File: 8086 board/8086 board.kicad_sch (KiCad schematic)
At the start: 37 parts, among them J1 8086 bus, U1 P8086-2, U2 74HC32

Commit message: PCB: different layout
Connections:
- net BUSALE: now also J1.21 (Pin_21); no longer J1.27 (Pin_27)
- net HLDA: now also J1.25 (Pin_25); no longer J1.23 (Pin_23)
- net HOLD: now also J1.28 (Pin_28); no longer J1.22 (Pin_22)
- net M\~{IO}: now also J1.23 (Pin_23); no longer J1.25 (Pin_25)
- net READY: now also J1.24 (Pin_24); no longer J1.26 (Pin_26)
- net ~{BHE}: now also J1.22 (Pin_22); no longer J1.28 (Pin_28)
- net ~{RD}: now also J1.27 (Pin_27); no longer J1.21 (Pin_21)
- net ~{WR}: now also J1.26 (Pin_26); no longer J1.24 (Pin_24)

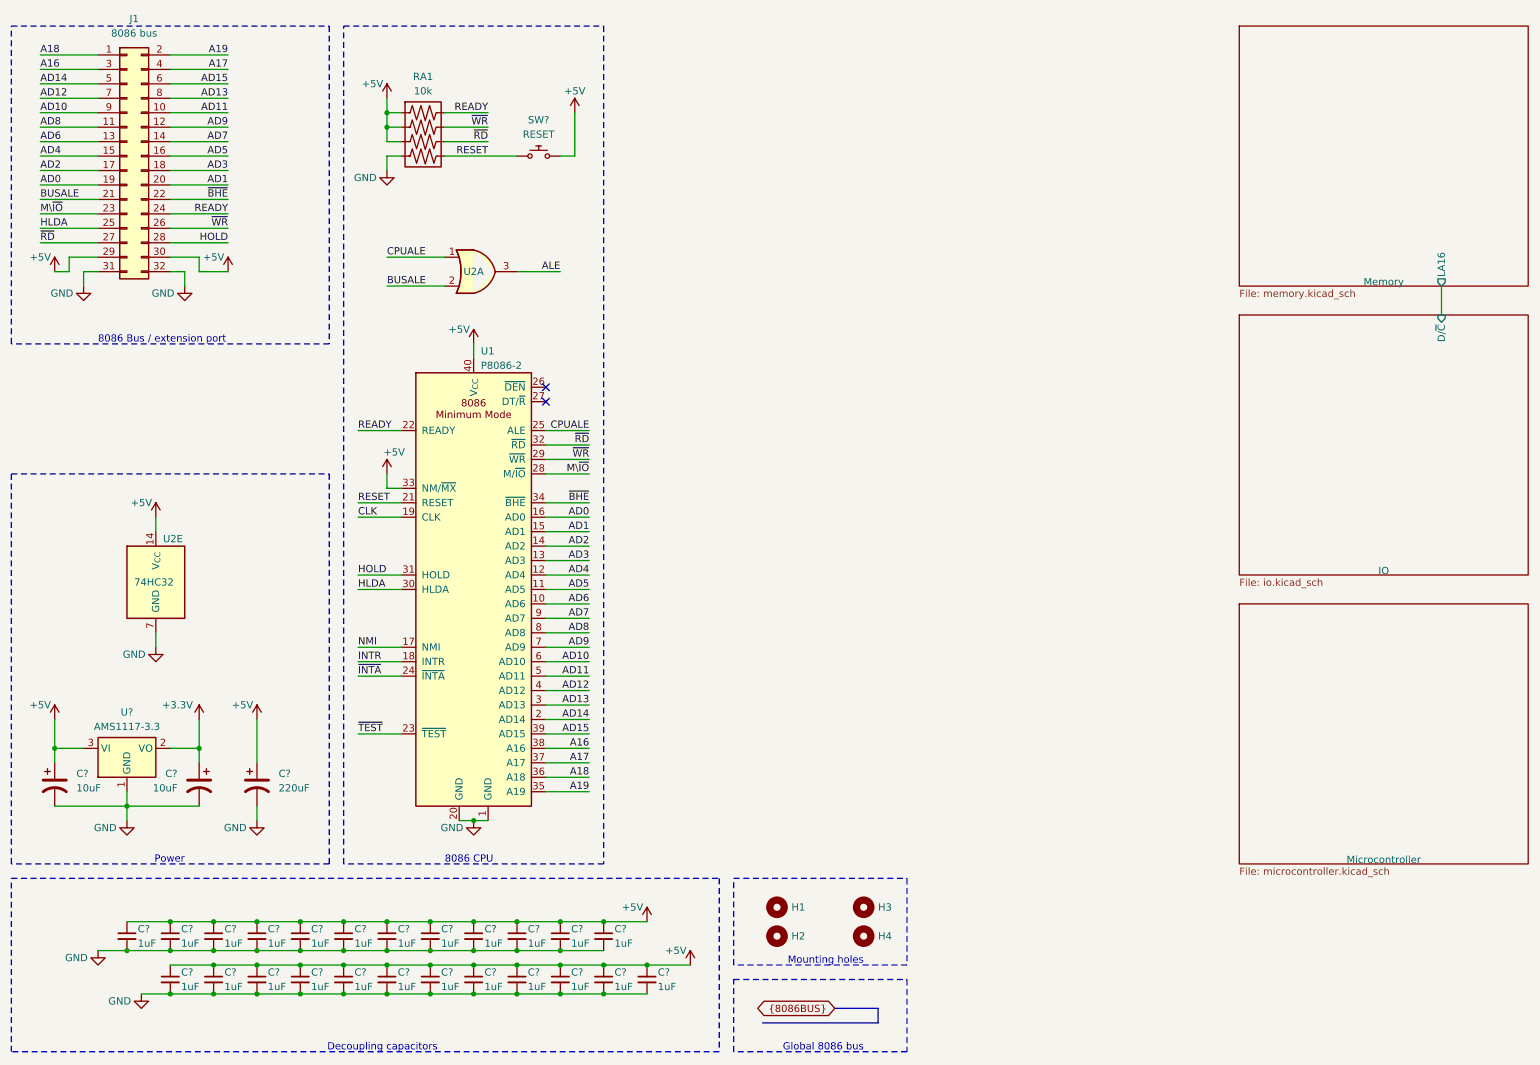
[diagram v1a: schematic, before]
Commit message: PCB: layout and routing of IO, shift registers, and MCU
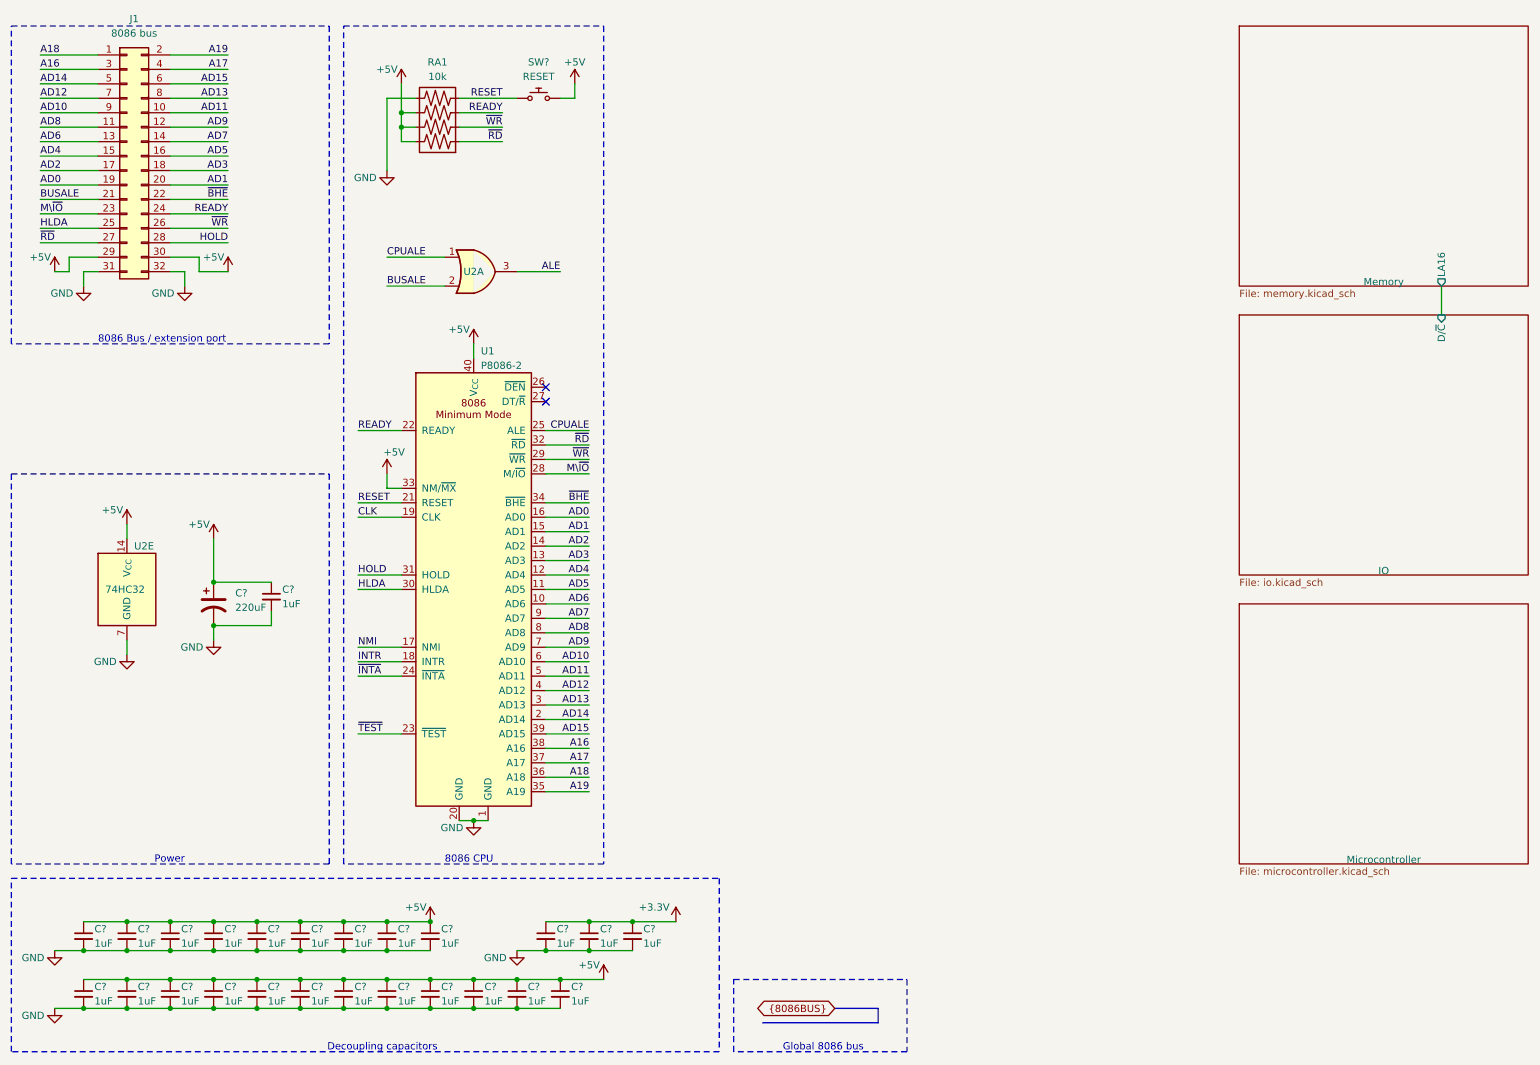
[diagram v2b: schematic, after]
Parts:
- removed C? (x2): 10uF, Capacitor_SMD:C_0603_1608Metric_Pad1.08x0.95mm_HandSolder, symbol Device:C_Polarized_US
- removed H1, H2, H3, H4: ~, MountingHole:MountingHole_3.2mm_M3, symbol Mechanical:MountingHole
- removed U?: AMS1117-3.3, Package_TO_SOT_SMD:SOT-223-3_TabPin2, symbol Regulator_Linear:AMS1117-3.3
- added C?: 1uF, Capacitor_SMD:C_0603_1608Metric_Pad1.08x0.95mm_HandSolder, symbol Device:C_Small
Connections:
- net +3.3V: now also C?.1, C?.1, C?.1
- net +5V: now also RA1.6, RA1.7, RA1.8, C?.1; no longer C?.1, C?.1, C?.1, RA1.1, RA1.2, RA1.3
- net GND: now also RA1.5, C?.2; no longer RA1.4
- net READY: now also RA1.3; no longer RA1.8
- net RESET: now also RA1.4; no longer RA1.5
- net ~{RD}: now also RA1.1; no longer RA1.6
- net ~{WR}: now also RA1.2; no longer RA1.7
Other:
- note removed: "Mounting holes"
- moved on the sheet: C?, RA1, SW?, U2E

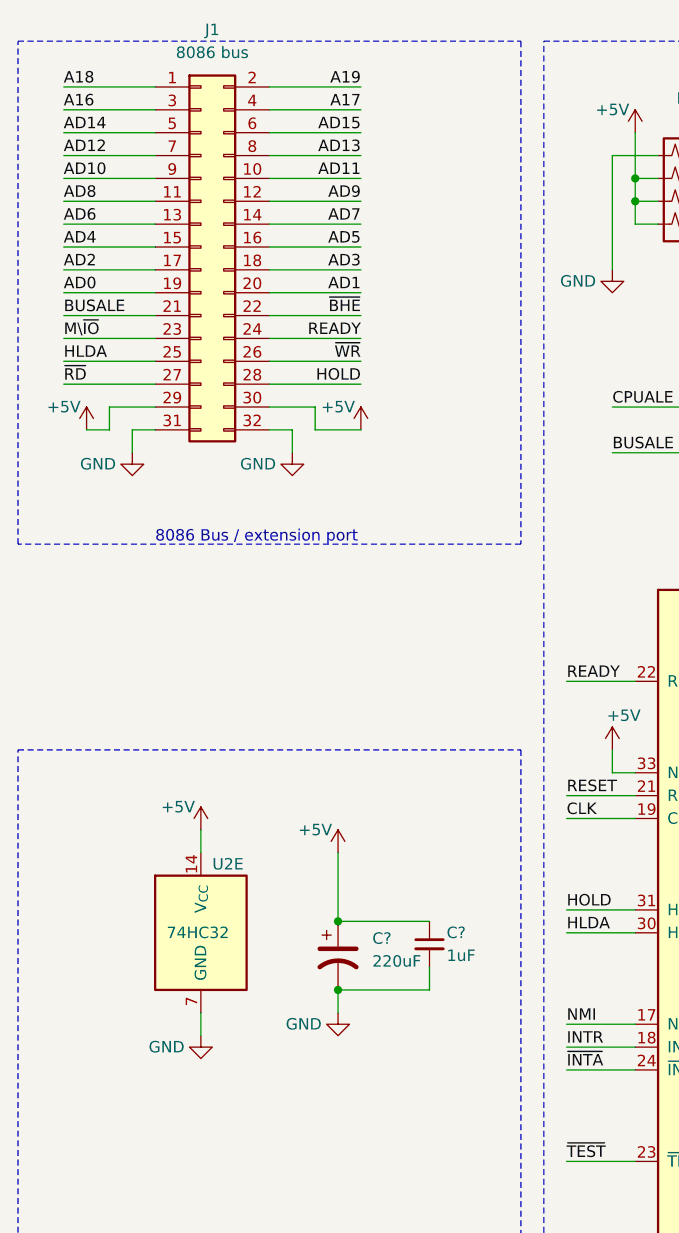
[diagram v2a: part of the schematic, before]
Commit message: small schematic  changes to better fit PCB
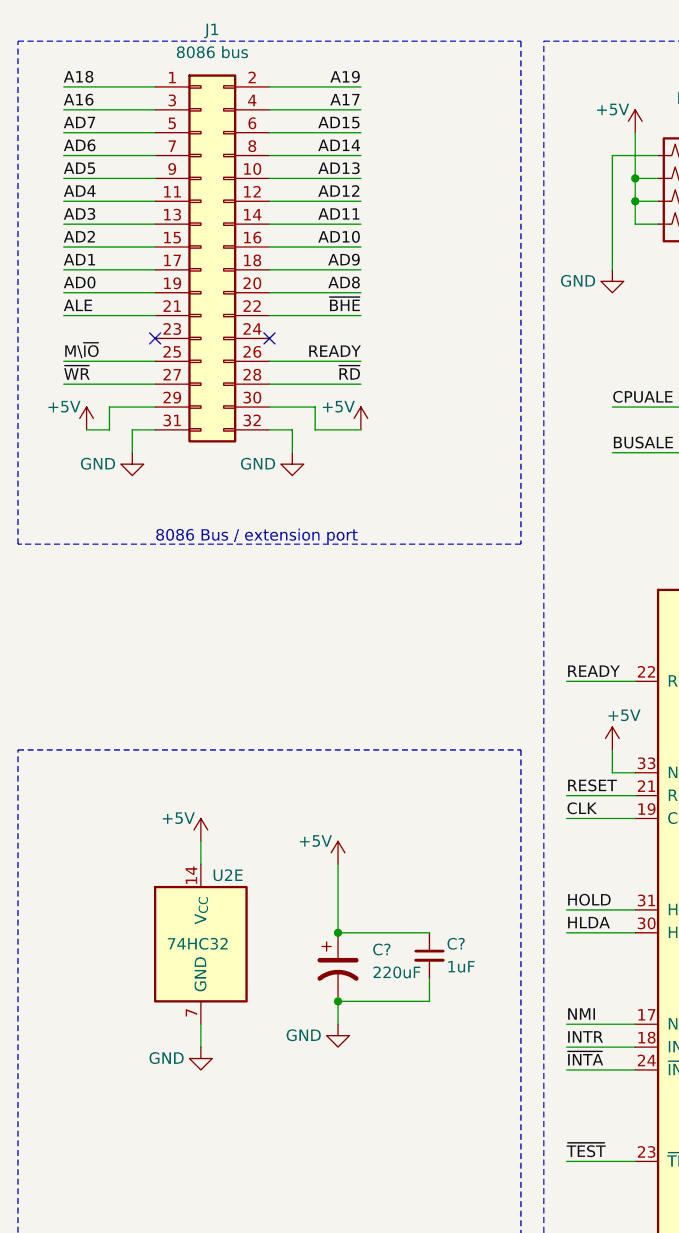
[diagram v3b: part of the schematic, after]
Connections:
- net AD1: now also J1.17 (Pin_17); no longer J1.20 (Pin_20)
- net AD10: now also J1.16 (Pin_16); no longer J1.9 (Pin_9)
- net AD11: now also J1.14 (Pin_14); no longer J1.10 (Pin_10)
- net AD12: now also J1.12 (Pin_12); no longer J1.7 (Pin_7)
- net AD13: now also J1.10 (Pin_10); no longer J1.8 (Pin_8)
- net AD14: now also J1.8 (Pin_8); no longer J1.5 (Pin_5)
- net AD2: now also J1.15 (Pin_15); no longer J1.17 (Pin_17)
- net AD3: now also J1.13 (Pin_13); no longer J1.18 (Pin_18)
- net AD4: now also J1.11 (Pin_11); no longer J1.15 (Pin_15)
- net AD5: now also J1.9 (Pin_9); no longer J1.16 (Pin_16)
- net AD6: now also J1.7 (Pin_7); no longer J1.13 (Pin_13)
- net AD7: now also J1.5 (Pin_5); no longer J1.14 (Pin_14)
- net AD8: now also J1.20 (Pin_20); no longer J1.11 (Pin_11)
- net AD9: now also J1.18 (Pin_18); no longer J1.12 (Pin_12)
- net ALE: now also J1.21 (Pin_21)
- net BUSALE: no longer J1.21 (Pin_21)
- net HLDA: no longer J1.25 (Pin_25)
- net HOLD: no longer J1.28 (Pin_28)
- net M\~{IO}: now also J1.25 (Pin_25); no longer J1.23 (Pin_23)
- net READY: now also J1.26 (Pin_26); no longer J1.24 (Pin_24)
- net ~{RD}: now also J1.28 (Pin_28); no longer J1.27 (Pin_27)
- net ~{WR}: now also J1.27 (Pin_27); no longer J1.26 (Pin_26)
- no-connect marks 2 -> 4
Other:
- moved on the sheet: C?, U2E

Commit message: schematic: fix LCD RD bug, geographical reannotation
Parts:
- SW?: value RESET -> ~; Key (none) -> ↻
- U22: renamed from U2; now in the parts list
- renumbered RA1 to RN7
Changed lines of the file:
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@@
   (title_block
     (title "8086 computer")
-    (date "2023.11.15")
-    (rev "V1.2.0")
+    (date "2023.11.19")
+    (rev "V1.3.0")
     (company "Eldad Hellerman")
     (comment 1 "Open Source: github.com/EldadHellerman/8086-computer")
@@
         )
         (path "/3749a875-289f-4484-aa3f-51b8984af853"
-          (reference "C12") (unit 1)
+          (reference "C16") (unit 1)
         )
       )
@@
         )
         (path "/3749a875-289f-4484-aa3f-51b8984af853"
-          (reference "C14") (unit 1)
+          (reference "C15") (unit 1)
         )
       )
@@
         )
         (path "/3749a875-289f-4484-aa3f-51b8984af853"
-          (reference "C11") (unit 1)
+          (reference "C17") (unit 1)
         )
       )
@@
         )
         (path "/3749a875-289f-4484-aa3f-51b8984af853"
-          (reference "C31") (unit 1)
+          (reference "C26") (unit 1)
         )
       )
@@
         )
         (path "/3749a875-289f-4484-aa3f-51b8984af853"
-          (reference "C29") (unit 1)
+          (reference "C22") (unit 1)
         )
       )
@@
         )
         (path "/3749a875-289f-4484-aa3f-51b8984af853"
-          (reference "C15") (unit 1)
+          (reference "C32") (unit 1)
         )
       )
@@
         )
         (path "/3749a875-289f-4484-aa3f-51b8984af853"
-          (reference "C26") (unit 1)
+          (reference "C20") (unit 1)
         )
       )
@@
         )
         (path "/3749a875-289f-4484-aa3f-51b8984af853"
-          (reference "C3") (unit 1)
+          (reference "C1") (unit 1)
         )
       )
@@
         )
         (path "/3749a875-289f-4484-aa3f-51b8984af853"
-          (reference "C24") (unit 1)
+          (reference "C30") (unit 1)
         )
       )
@@
         )
         (path "/3749a875-289f-4484-aa3f-51b8984af853"
-          (reference "C19") (unit 1)
+          (reference "C7") (unit 1)
         )
       )
@@
         )
         (path "/3749a875-289f-4484-aa3f-51b8984af853"
-          (reference "C10") (unit 1)
+          (reference "C14") (unit 1)
         )
       )
@@
         )
         (path "/3749a875-289f-4484-aa3f-51b8984af853"
-          (reference "C8") (unit 1)
+          (reference "C12") (unit 1)
         )
       )
@@
         )
         (path "/3749a875-289f-4484-aa3f-51b8984af853"
-          (reference "C13") (unit 1)
+          (reference "C29") (unit 1)
         )
       )
@@
         )
         (path "/3749a875-289f-4484-aa3f-51b8984af853"
-          (reference "C18") (unit 1)
+          (reference "C6") (unit 1)
         )
       )
@@
         )
         (path "/3749a875-289f-4484-aa3f-51b8984af853"
-          (reference "C23") (unit 1)
+          (reference "C11") (unit 1)
         )
       )
@@
   (symbol (lib_id "8086PC:R_Array_4") (at 91.44 33.02 180) (unit 1)
     (in_bom yes) (on_board yes) (dnp no) (fields_autoplaced)
-    (property "Reference" "RA1" (at 90.17 21.59 0)
+    (property "Reference" "RN7" (at 90.17 21.59 0)
       (effects (font (size 1.27 1.27)))
     )
@@
       (project "8086 board"
         (path "/3749a875-289f-4484-aa3f-51b8984af853"
-          (reference "RA1") (unit 1)
+          (reference "RN7") (unit 1)
         )
       )
@@
         )
         (path "/3749a875-289f-4484-aa3f-51b8984af853"
-          (reference "C17") (unit 1)
+          (reference "C5") (unit 1)
         )
       )
@@
         )
         (path "/3749a875-289f-4484-aa3f-51b8984af853"
-          (reference "C30") (unit 1)
+          (reference "C19") (unit 1)
         )
       )
@@
         )
         (path "/3749a875-289f-4484-aa3f-51b8984af853"
-          (reference "C27") (unit 1)
+          (reference "C21") (unit 1)
         )
       )
@@
         )
         (path "/3749a875-289f-4484-aa3f-51b8984af853"
-          (reference "C9") (unit 1)
+          (reference "C13") (unit 1)
         )
       )
@@
         )
         (path "/3749a875-289f-4484-aa3f-51b8984af853"
-          (reference "C16") (unit 1)
+          (reference "C31") (unit 1)
         )
       )
@@
   )
   (symbol (lib_id "8086PC:74HC32") (at 96.52 58.42 0) (unit 1)
-    (in_bom no) (on_board yes) (dnp no)
-    (property "Reference" "U2" (at 96.52 58.42 0)
+    (in_bom yes) (on_board yes) (dnp no)
+    (property "Reference" "U22" (at 96.52 58.42 0)
       (effects (font (size 1.27 1.27)))
     )
@@
       (project "8086 board"
         (path "/3749a875-289f-4484-aa3f-51b8984af853"
-          (reference "U2") (unit 1)
+          (reference "U22") (unit 1)
         )
       )
@@
   )
   (symbol (lib_id "8086PC:74HC32") (at 35.56 114.3 0) (unit 5)
-    (in_bom no) (on_board yes) (dnp no)
-    (property "Reference" "U2" (at 36.83 107.95 0)
+    (in_bom yes) (on_board yes) (dnp no)
+    (property "Reference" "U22" (at 36.83 107.95 0)
       (effects (font (size 1.27 1.27)) (justify left))
     )
@@
       (project "8086 board"
         (path "/3749a875-289f-4484-aa3f-51b8984af853"
-          (reference "U2") (unit 5)
+          (reference "U22") (unit 5)
         )
       )
@@
         )
         (path "/3749a875-289f-4484-aa3f-51b8984af853"
-          (reference "C20") (unit 1)
+          (reference "C10") (unit 1)
         )
       )
@@
   )
   (symbol (lib_id "8086PC:SW_Push") (at 109.22 27.94 0) (mirror y) (unit 1)
-    (in_bom yes) (on_board yes) (dnp no) (fields_autoplaced)
+    (in_bom yes) (on_board yes) (dnp no)
     (property "Reference" "SW?" (at 107.95 21.59 0)
       (effects (font (size 1.27 1.27)))
     )
-    (property "Value" "RESET" (at 107.95 24.13 0)
+    (property "Value" "~" (at 107.95 24.13 0)
       (effects (font (size 1.27 1.27)))
     )
@@
     (property "Datasheet" "~" (at 107.95 27.94 0)
       (effects (font (size 1.27 1.27)) hide)
+    )
+    (property "Key" "↻" (at 107.95 24.13 0)
+      (effects (font (size 1.27 1.27)))
     )
     (pin "1")
@@
         )
         (path "/3749a875-289f-4484-aa3f-51b8984af853"
-          (reference "C21") (unit 1)
+          (reference "C8") (unit 1)
         )
       )
@@
         )
         (path "/3749a875-289f-4484-aa3f-51b8984af853"
-          (reference "C28") (unit 1)
+          (reference "C23") (unit 1)
         )
       )
@@
         )
         (path "/3749a875-289f-4484-aa3f-51b8984af853"
-          (reference "C22") (unit 1)
+          (reference "C9") (unit 1)
         )
       )
@@
         )
         (path "/3749a875-289f-4484-aa3f-51b8984af853"
-          (reference "C32") (unit 1)
+          (reference "C3") (unit 1)
         )
       )
@@
         )
         (path "/3749a875-289f-4484-aa3f-51b8984af853"
-          (reference "C25") (unit 1)
-        )
-      )
+          (reference "C27") (unit 1)
+        )
+      )

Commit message: PCB: move to kicad 8
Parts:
- gave numbers to parts that had none: 27
